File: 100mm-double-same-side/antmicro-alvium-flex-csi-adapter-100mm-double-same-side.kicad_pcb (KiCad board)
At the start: 2 copper layers, 81.8 x 100.1 mm, 3 parts, among them J1 WE_687622100002_FLEX, J2 WE_687622100002_FLEX, J3 WE_687650100002_FLEX

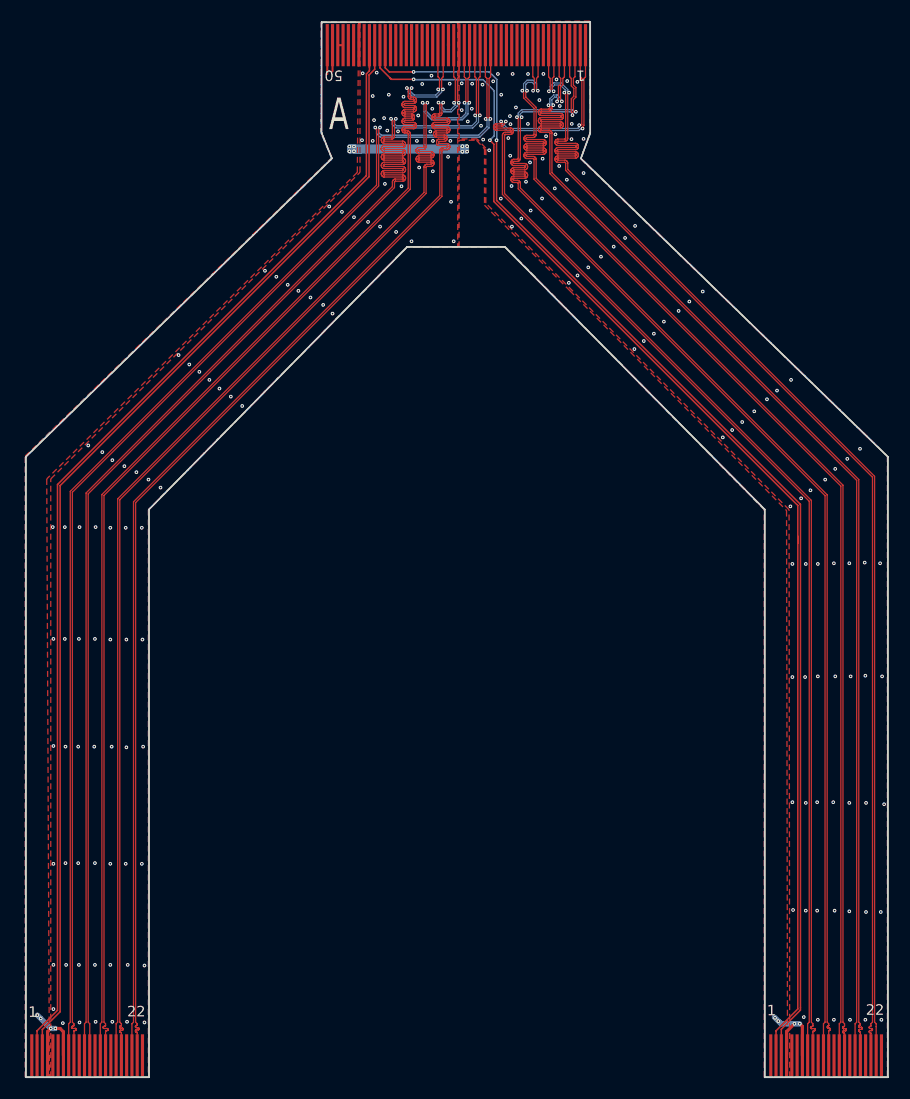
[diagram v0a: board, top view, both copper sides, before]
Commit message: 100mm-double-same: Add signage
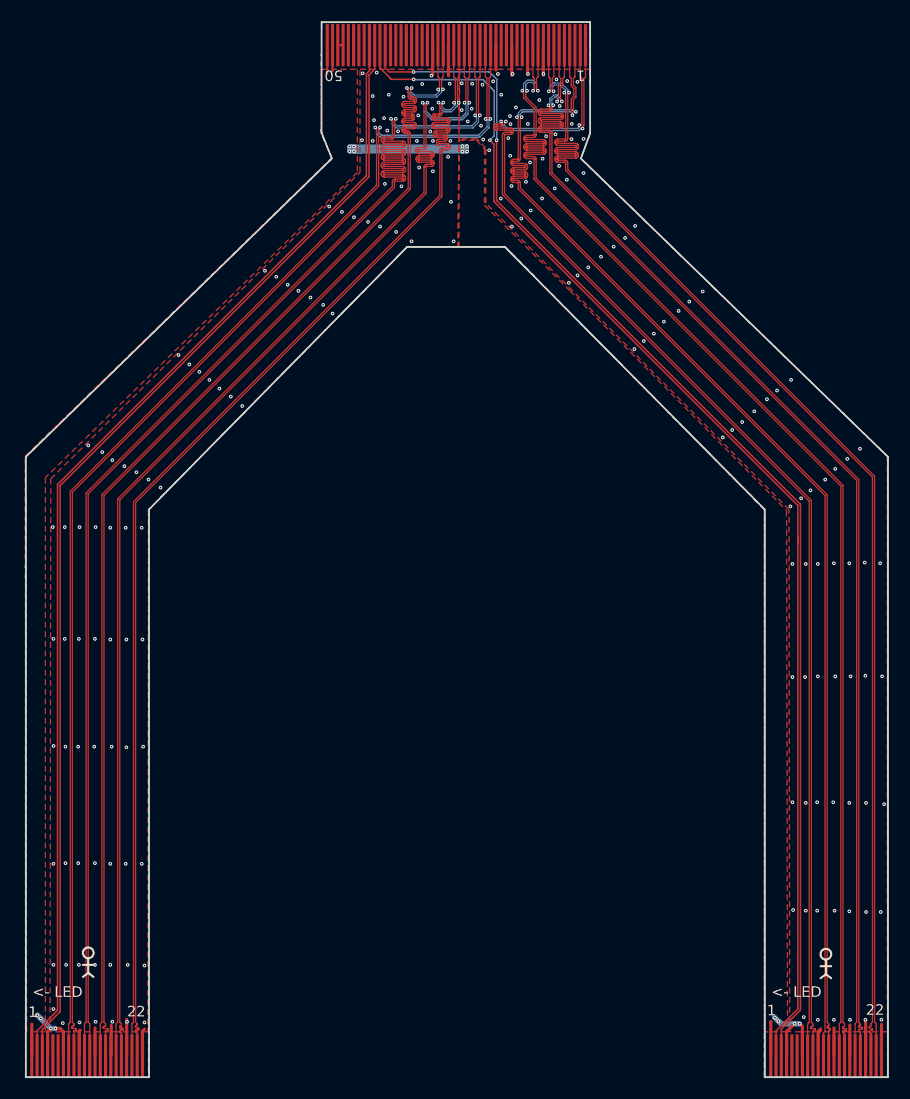
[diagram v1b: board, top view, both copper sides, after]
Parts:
- added N1: oshw_logo, antmicro-alvium-flex-csi-adapter-footprints:oshw-logo, B.Cu at (157.9, 101.9)
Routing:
- net /F1_GND: track 0.18 -> 46.3 mm
- net /F1_5V: track 46.6 -> 52.8 mm
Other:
- board text added: "<- LED"
- board text added: "Antmicro Alvium Flex CSI Adapter 100mm double same side contacts Rev. 1.0.0"
- board text removed: "A"

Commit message: Add NMOS transistors for camera triggering in 100mm double same side variant
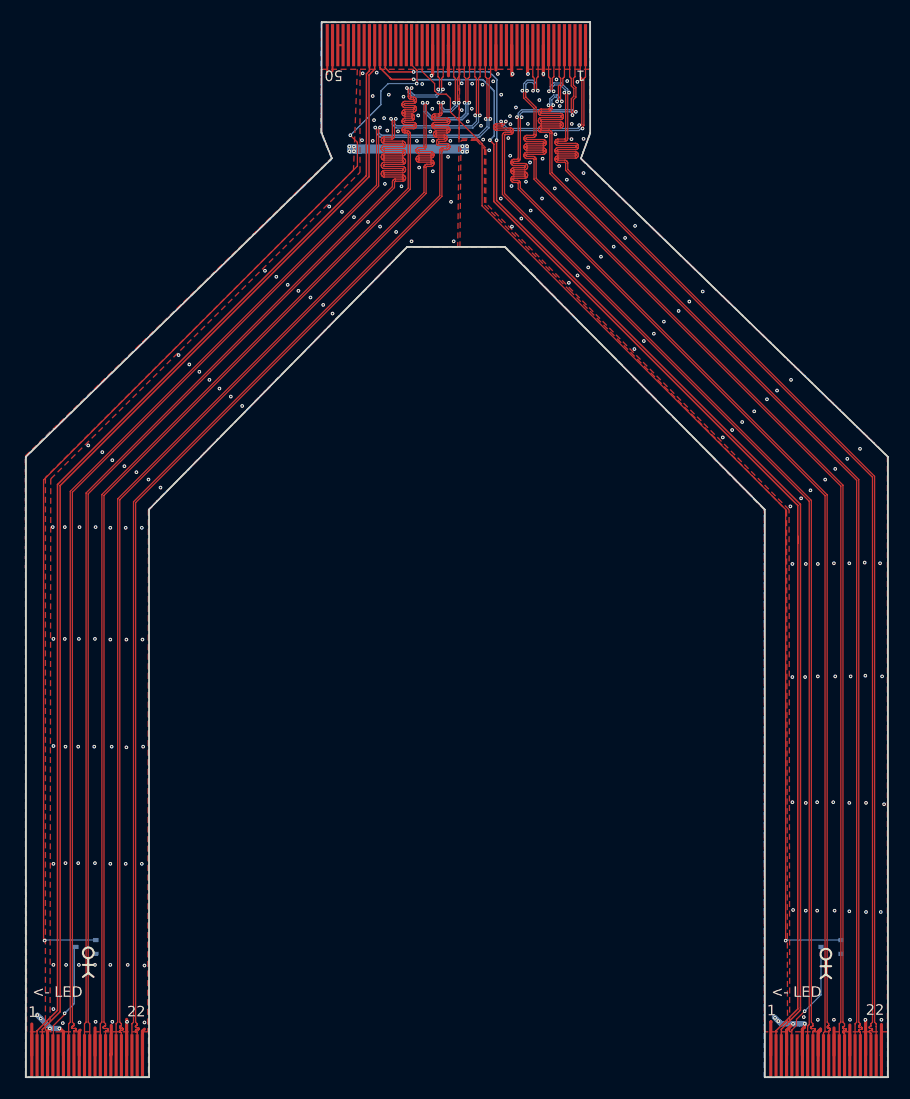
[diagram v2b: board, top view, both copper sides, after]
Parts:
- added Q1: BSS138APW, antmicro-alvium-flex-csi-adapter-footprints:SC70-3, B.Cu at (158.6, 106.5)
- added Q2: BSS138APW, antmicro-alvium-flex-csi-adapter-footprints:SC70-3, B.Cu at (87.9, 106.5)
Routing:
- net /F1_C2_VSYNC: track 0.00 -> 106.9 mm, vias 0 -> 3
- net /F1_C1_VSYNC: track 0.00 -> 105.0 mm, vias 0 -> 1
- net /F1_C1_GPIO2: track 0.00 -> 11.4 mm, vias 0 -> 1
- net /F1_C2_GPIO2: track 0.00 -> 11.2 mm, vias 0 -> 1
- net /F1_5V: track 52.8 -> 54.0 mm
